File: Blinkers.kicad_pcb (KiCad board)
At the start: 2 copper layers, 238 x 45 mm, 218 parts, among them J1 12V, J2 A1, J3 gnd, J4 A1, J5 A1, J6 A1, J7 A1, J8 A1, Q1 Q_NMOS_DGS, Q2 Q_NMOS_DGS, Q3 Q_NMOS_DGS, Q4 Q_NMOS_DGS, Q5 Q_NMOS_DGS, Q6 Q_NMOS_DGS

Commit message: Separated VCC and GND
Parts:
- moved J1 53.6 mm to (266.7, 91.4)
- moved J3 52.6 mm to (266.7, 127.0)
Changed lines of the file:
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@@
   )
   (module Socket_Strips:Socket_Strip_Straight_1x01_Pitch2.54mm (layer F.Cu)
-    (at 214.63 104.14)
+    (at 266.7 91.44)
     (descr "Through hole straight socket strip, 1x01, 2.54mm pitch, single row")
     (tags "Through hole socket strip THT 1x01 2.54mm single row")
@@
   )
   (module Socket_Strips:Socket_Strip_Straight_1x01_Pitch2.54mm (layer F.Cu)
-    (at 214.63 119.38)
+    (at 266.7 127)
     (descr "Through hole straight socket strip, 1x01, 2.54mm pitch, single row")
     (tags "Through hole socket strip THT 1x01 2.54mm single row")

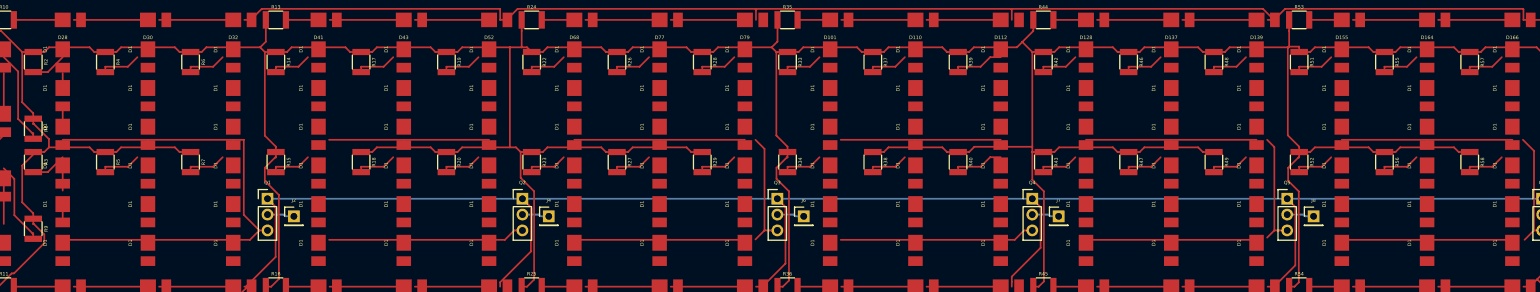
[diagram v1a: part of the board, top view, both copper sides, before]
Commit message: Changed footprint designators.
The footprint designators had been all changed to "D1" after using the array tool. In the future we'll need to use a script unless the array tool is fixed.
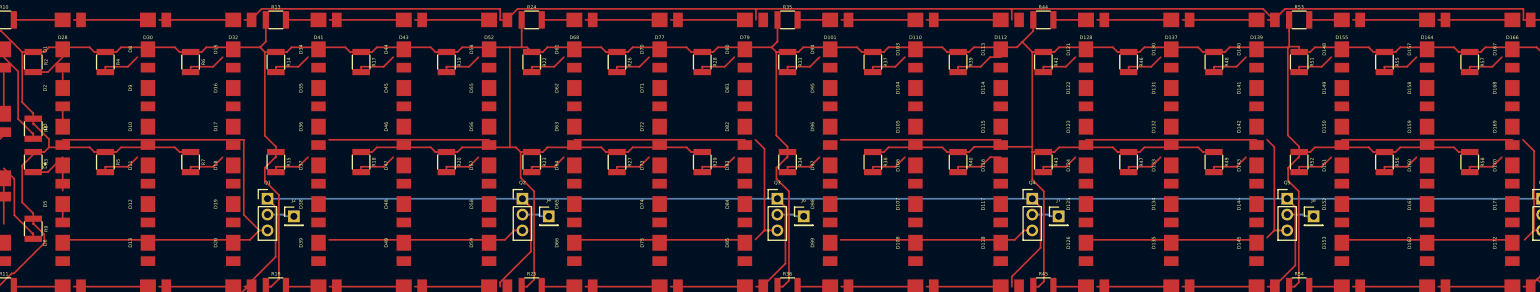
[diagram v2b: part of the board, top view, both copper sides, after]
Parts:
- renumbered D1 to D10, D1 to D103, D1 to D104, D1 to D105, D1 to D106, D1 to D107, D1 to D108, D1 to D11, D1 to D113, D1 to D114, D1 to D115, D1 to D116, D1 to D117, D1 to D118, D1 to D12, D1 to D121, D1 to D122, D1 to D123, D1 to D124, D1 to D125, D1 to D126, D1 to D13, D1 to D130, D1 to D131, D1 to D132, D1 to D133, D1 to D134, D1 to D135, D1 to D140, D1 to D141, D1 to D142, D1 to D143, D1 to D144, D1 to D145, D1 to D148, D1 to D149, D1 to D15, D1 to D150, D1 to D151, D1 to D152, D1 to D153, D1 to D157, D1 to D158, D1 to D159, D1 to D16, D1 to D160, D1 to D161, D1 to D162, D1 to D167, D1 to D168, D1 to D169, D1 to D17, D1 to D170, D1 to D171, D1 to D172, D1 to D18, D1 to D19, D1 to D2, D1 to D20, D1 to D3, D1 to D34, D1 to D35, D1 to D36, D1 to D37, D1 to D38, D1 to D39, D1 to D4, D1 to D44, D1 to D45, D1 to D46, D1 to D47, D1 to D48, D1 to D49, D1 to D5, D1 to D54, D1 to D55, D1 to D56, D1 to D57, D1 to D58, D1 to D59, D1 to D6, D1 to D61, D1 to D62, D1 to D63, D1 to D64, D1 to D65, D1 to D66, D1 to D70, D1 to D71, D1 to D72, D1 to D73, D1 to D74, D1 to D75, D1 to D8, D1 to D80, D1 to D81, D1 to D82, D1 to D83, D1 to D84, D1 to D85, D1 to D9, D1 to D94, D1 to D95, D1 to D96, D1 to D97, D1 to D98, D1 to D99

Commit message: Final board layout, without bottom row of internal LEDs and no separate inputs for outer ring.
Last upload didn't seem to work with the traces. This one includes the traces.
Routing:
- net Net-(D1-Pad2): track 7.66 -> 1271.5 mm, vias 0 -> 2
- net Net-(D1-Pad1): track 81.5 -> 1268.9 mm
- net 12V: track 673.9 -> 938.1 mm, vias 0 -> 1
- net Net-(D10-Pad1): track 70.3 -> 0.00 mm
- net Net-(D36-Pad1): track 51.6 -> 0.00 mm
- net Net-(D105-Pad1): track 51.4 -> 0.00 mm
- net GND: track 609.1 -> 557.8 mm, vias 0 -> 6
- net Net-(D63-Pad1): track 42.0 -> 0.00 mm
- net Net-(D123-Pad1): track 41.5 -> 0.00 mm
- net Net-(D150-Pad1): track 41.5 -> 0.00 mm
- net Net-(D91-Pad1): track 0.00 -> 15.3 mm
- net Net-(D25-Pad1): track 0.00 -> 15.1 mm
- net Net-(D22-Pad1): track 0.00 -> 14.7 mm
- net Net-(D88-Pad1): track 0.00 -> 14.7 mm
- net Net-(D25-Pad2): track 17.7 -> 7.91 mm
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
